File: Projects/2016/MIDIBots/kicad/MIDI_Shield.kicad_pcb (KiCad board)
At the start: 2 copper layers, 69 parts, among them IC1 PC900V, K1 SRVO1, K2 SRVO2, K3 SRVO3, P10 A3, P11 A4, P12 AUX_12V, P13 AUX_12V, P14 AUX_5V, P15 AUX_5V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

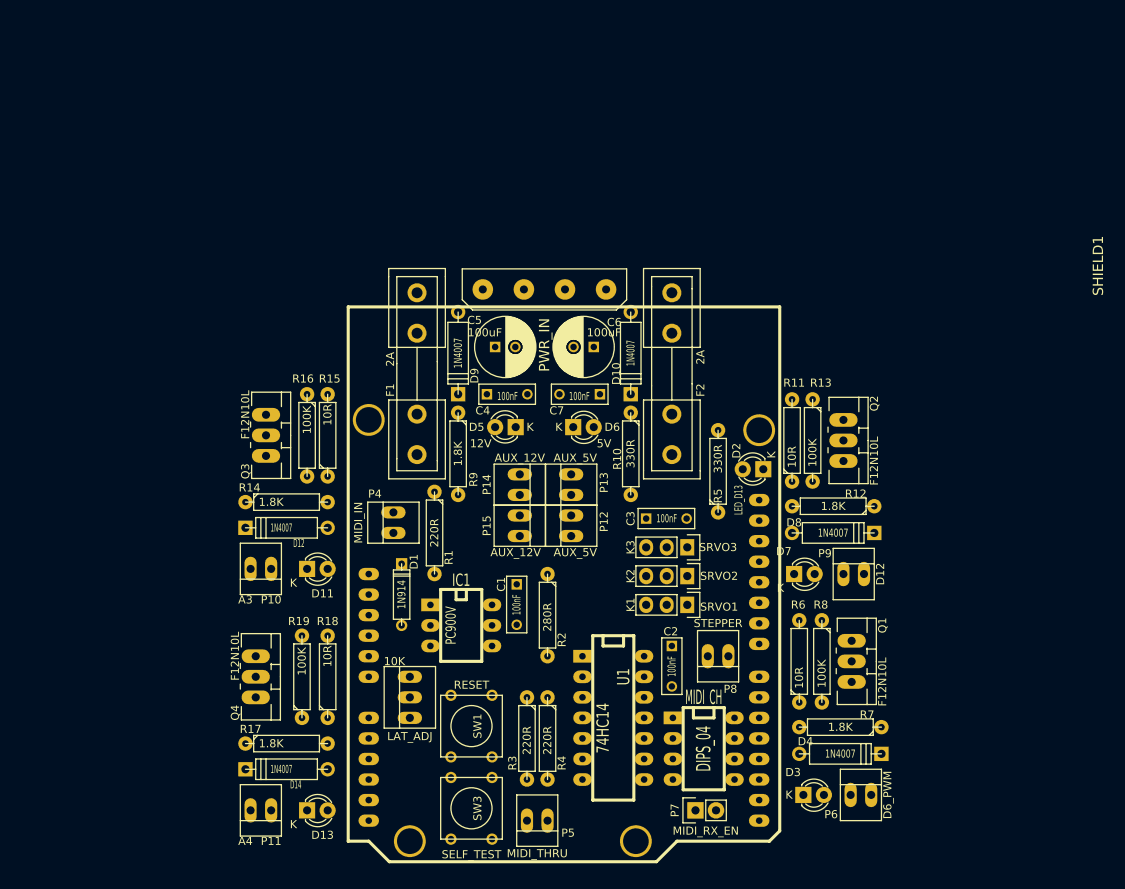
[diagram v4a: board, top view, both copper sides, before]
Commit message: Initial rough attempts at routing traces
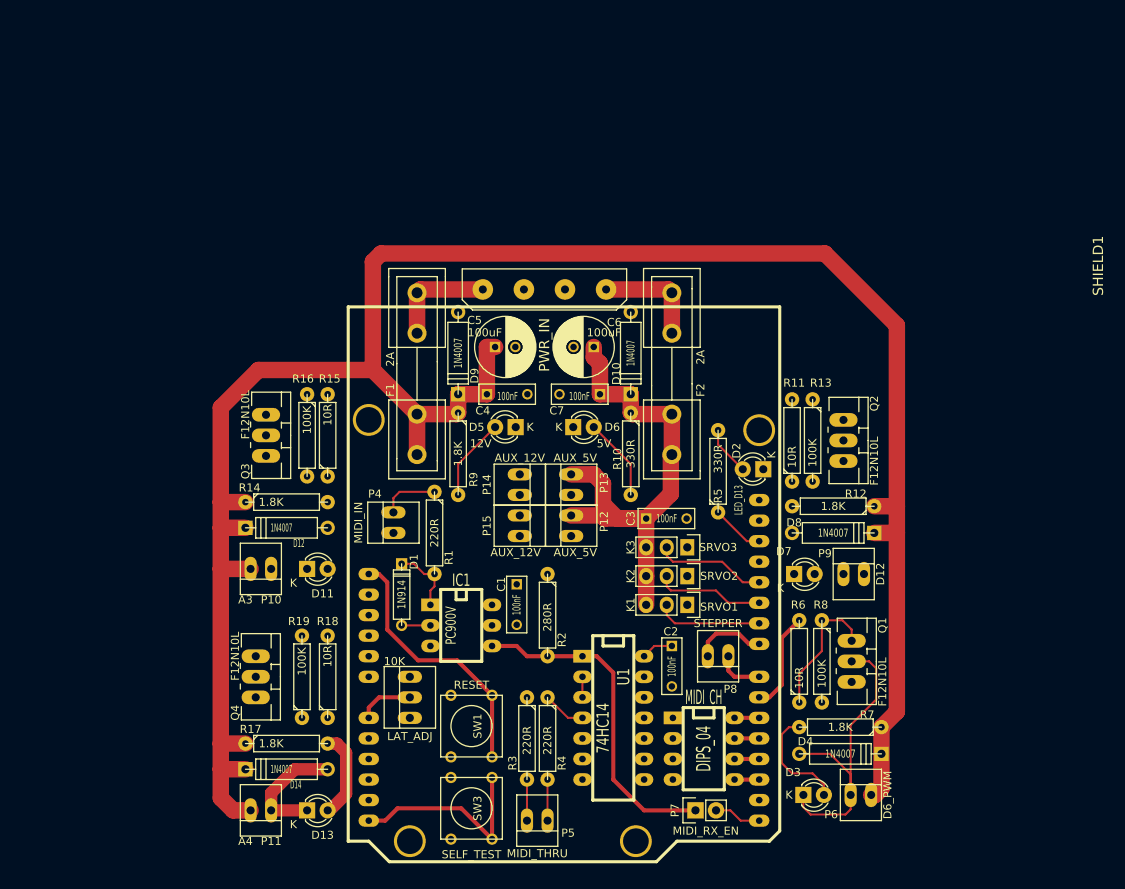
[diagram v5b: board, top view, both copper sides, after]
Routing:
- net +12V: track 0.00 -> 267.2 mm
- net +5V: track 0.00 -> 64.7 mm
- net /MIDI_IN_TTL: track 0.00 -> 41.3 mm
- net Net-(D3-Pad1): track 0.00 -> 40.1 mm
- net /RESET: track 0.00 -> 32.5 mm
- net /SELF_TEST: track 0.00 -> 25.1 mm
- net Net-(Q1-Pad1): track 0.00 -> 16.9 mm
- net Net-(D13-Pad1): track 0.00 -> 15.9 mm
- net /SERVO_3: track 0.00 -> 13.8 mm
- net Net-(D3-Pad2): track 0.00 -> 13.7 mm
- net /SERVO_2: track 0.00 -> 13.5 mm
- net Net-(F2-Pad1): track 0.00 -> 13.3 mm
- net Net-(F1-Pad2): track 0.00 -> 13.3 mm
- net /SERVO_1: track 0.00 -> 13.1 mm
- net /MOSFET_1_PWM: track 0.00 -> 12.3 mm
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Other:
- net class Logic added: clearance 0.254, trace_width 0.508, via_dia 0.889, via_drill 0.635
- net class Power added: clearance 0.254, trace_width 1.524, via_dia 0.889, via_drill 0.635
- net class Power_Distribution added: clearance 0.254, trace_width 2.032, via_dia 0.889, via_drill 0.635

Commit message: Rough edge cut test
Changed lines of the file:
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@@
   (module arduino_shields:ARDUINO_SHIELD locked (layer F.Cu)
     (at 71.12 81.28 270)
-    (fp_text reference SHIELD1 (at -5.08 -92.71 270) (layer F.SilkS)
+    (fp_text reference SHIELD1 (at -13.208 -24.892 360) (layer F.SilkS)
       (effects (font (thickness 0.3048)))
     )
-    (fp_text value ARDUINO_SHIELD (at 0 -95.25 270) (layer F.SilkS) hide
+    (fp_text value ARDUINO_SHIELD (at -10.668 -25.146 360) (layer F.SilkS) hide
       (effects (font (thickness 0.3048)))
     )
@@
   (segment (start 124.714 128.016) (end 124.714 122.174) (width 0.508) (layer F.Cu) (net 44))
   (segment (start 124.714 122.174) (end 126.873 120.015) (width 0.508) (layer F.Cu) (net 44))
+  (zone (net 0) (net_name "") (layer Edge.Cuts) (hatch edge 0.508)
+    (connect_pads (clearance 0.508))
+    (min_thickness 0.254)
+    (fill yes (arc_segments 16) (thermal_gap 0.508) (thermal_bridge_width 0.508))
+    (polygon
+      (pts
+        (xy 131.572 72.39) (xy 142.748 83.566) (xy 142.748 144.78) (xy 136.906 150.622) (xy 59.69 150.622)
+        (xy 52.07 143.002) (xy 52.07 89.916) (xy 69.596 72.39) (xy 95.758 65.024)
+      )
+    )
+  )
 )

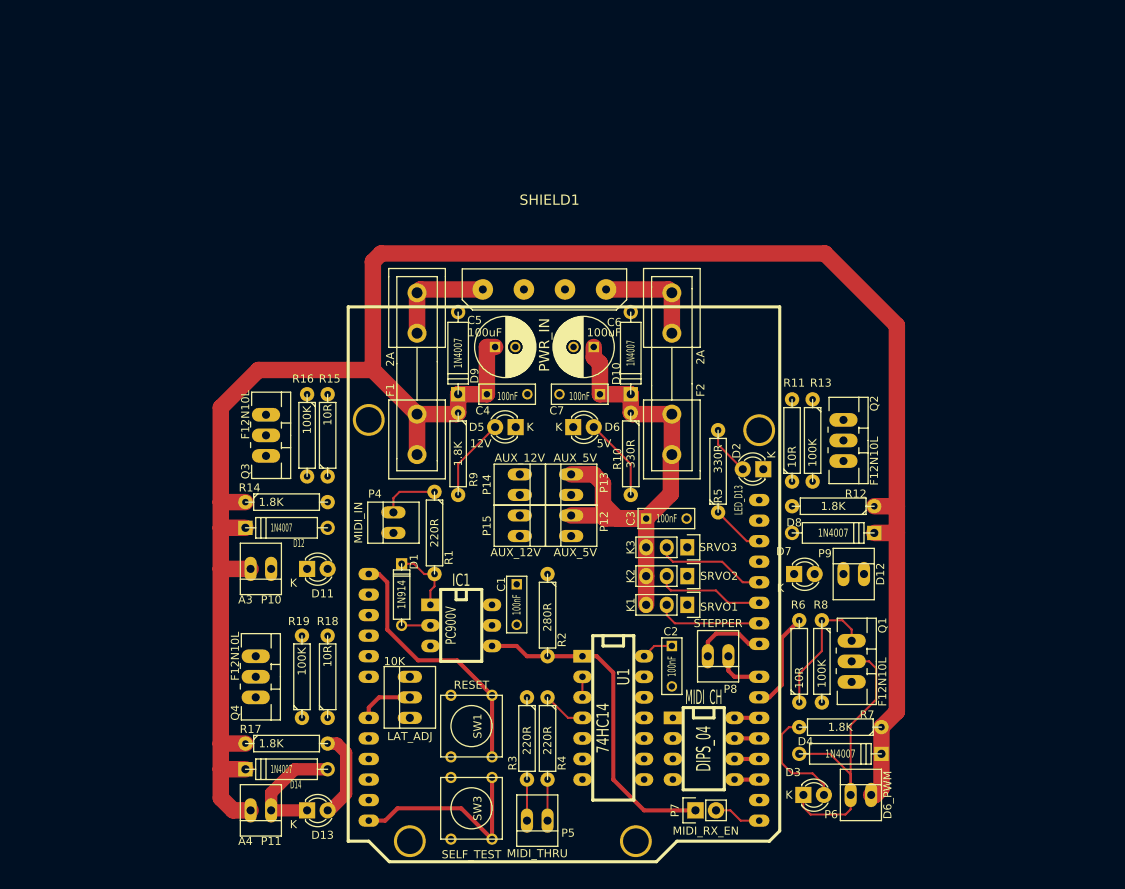
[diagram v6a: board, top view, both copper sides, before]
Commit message: [Y] Added Current_Loop track style [Y] Assigned some more track styles and ran a few additional tracks
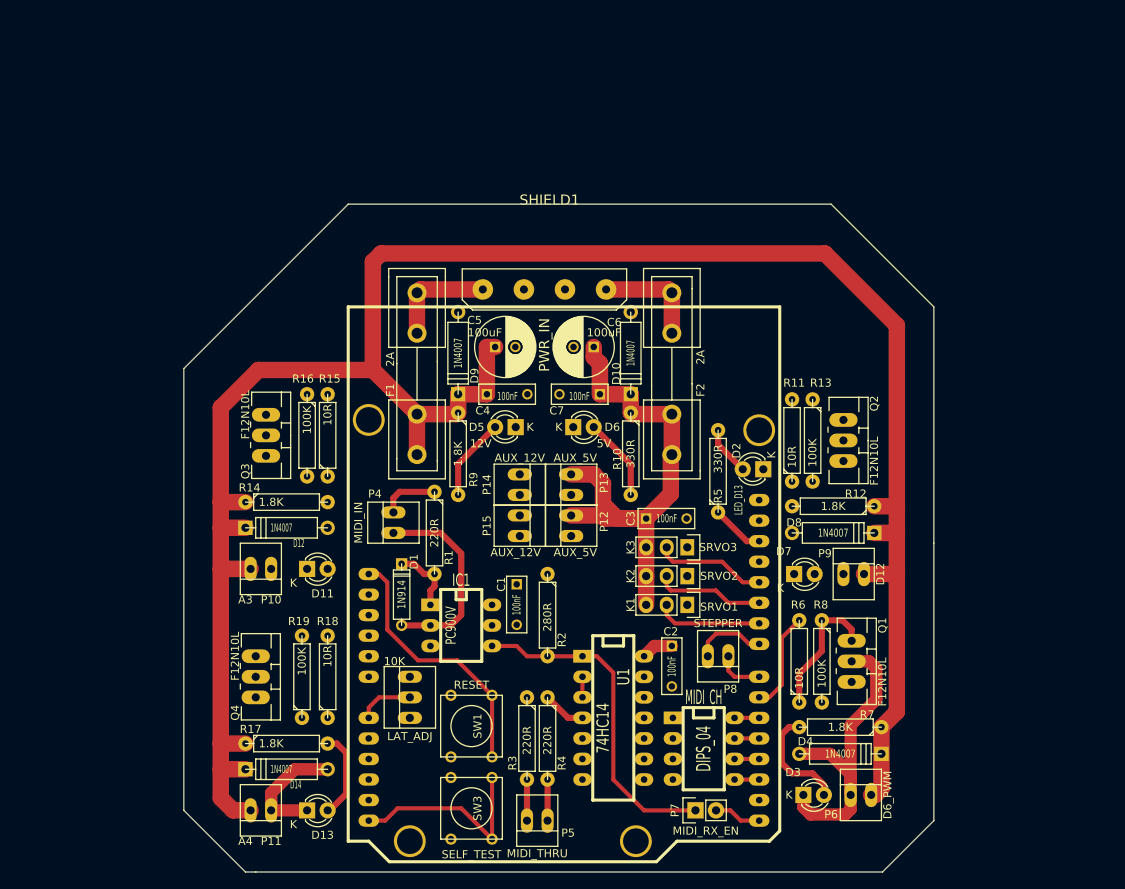
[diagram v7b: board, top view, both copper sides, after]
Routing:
- net Net-(D1-Pad2): track 3.56 -> 24.9 mm
- net +12V: track 267.2 -> 271.3 mm
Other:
- board outline added: 92.7 x 82.5 mm
- net class Current_Loop added: clearance 0.254, trace_width 0.762, via_dia 0.889, via_drill 0.635

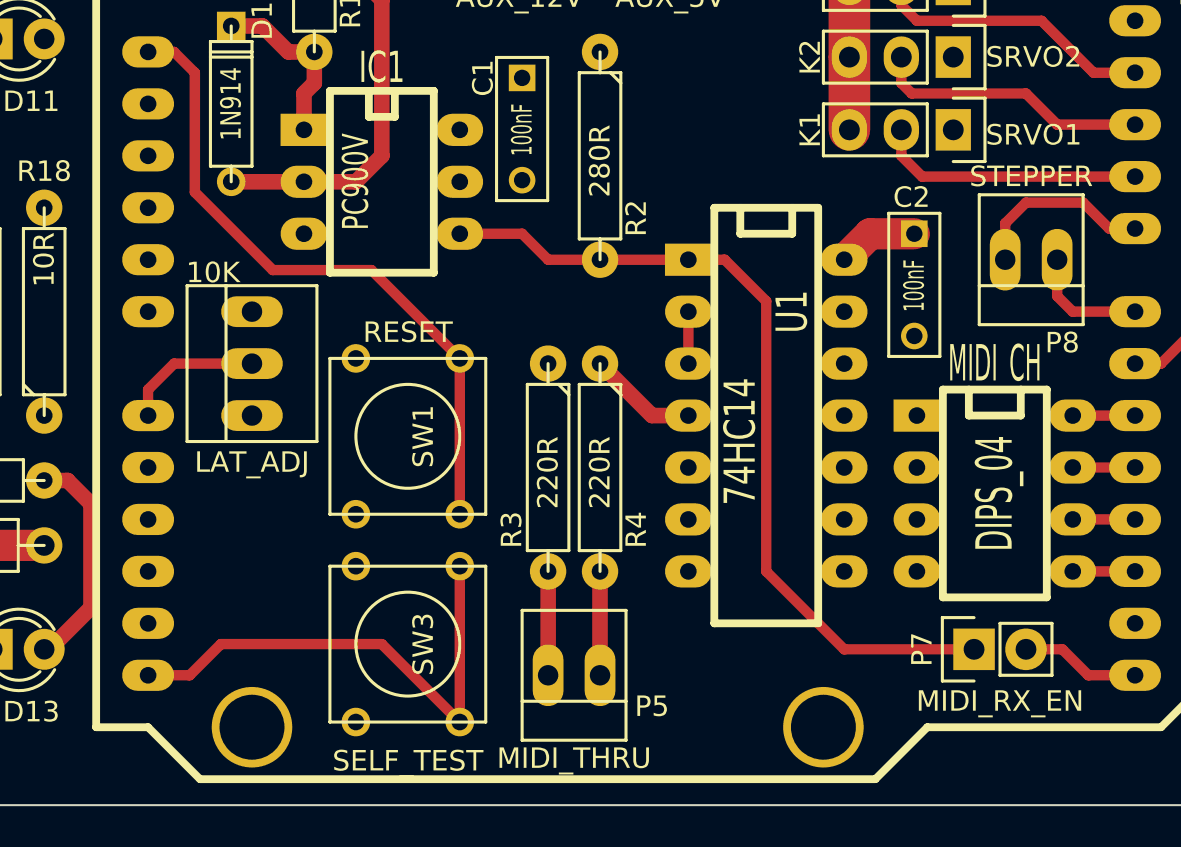
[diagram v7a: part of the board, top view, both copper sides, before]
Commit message: [Y] Remap pins for MOSFET 3 and 4 to make PCB routing easier [Y] Break out remaining Arduino pins (there's only 2!) and put header with a GND in the bottom left corner. [Y] Fixed unexpected mess with use of old DIP socket footprints [Y] Various footprints remapped [Y] SELF_TEST track re-routed slightly
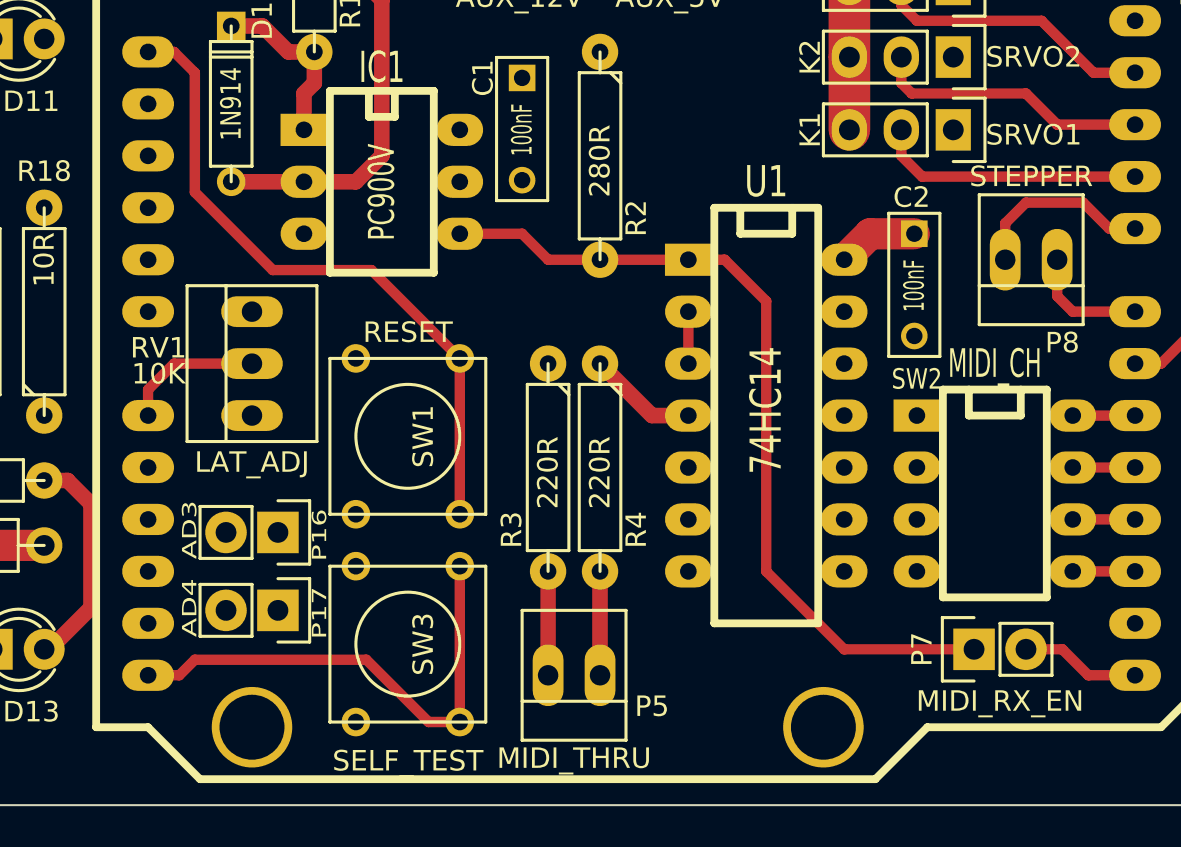
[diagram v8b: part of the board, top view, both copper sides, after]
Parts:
- removed LAT_ADJ: 10K, Connect:PINHEAD1-3
- removed MIDI_CH: DIPS_04, dip_sockets:DIP-8__300_ELL
- added P16: AD3, Pin_Headers:Pin_Header_Straight_1x02, F.Cu at (80.0, 137.8)
- added P17: AD4, Pin_Headers:Pin_Header_Straight_1x02, F.Cu at (80.0, 141.6)
- added RV1: 10K, Connect:PINHEAD1-3, F.Cu at (78.7, 129.5)
- added SW2: MIDI_CH, infomechatronics:DIP-8__300_ELL, F.Cu at (115.1, 135.9)
- IC1: footprint dip_sockets:DIP-6__300_ELL -> infomechatronics:DIP-6__300_ELL
- U1: footprint dip_sockets:DIP-14__300_ELL -> infomechatronics:DIP-14__300_ELL
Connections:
- SHIELD1 pad AD1: (no net) -> /MOSFET_3
- SHIELD1 pad AD2: (no net) -> /MOSFET_4
- SHIELD1 pad AD3: /MOSFET_3 -> /AD3
- SHIELD1 pad AD4: /MOSFET_4 -> /AD4
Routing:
- net /SELF_TEST: track 25.1 -> 24.4 mm
